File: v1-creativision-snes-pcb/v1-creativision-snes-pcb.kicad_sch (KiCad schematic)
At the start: 11 parts, among them J1 Left Joystick, J2 Right Joystick, J3 Power Entry, J4 PS/2 Keyboard, J5 SNES, SW1 Reset Pico, U1 Pico

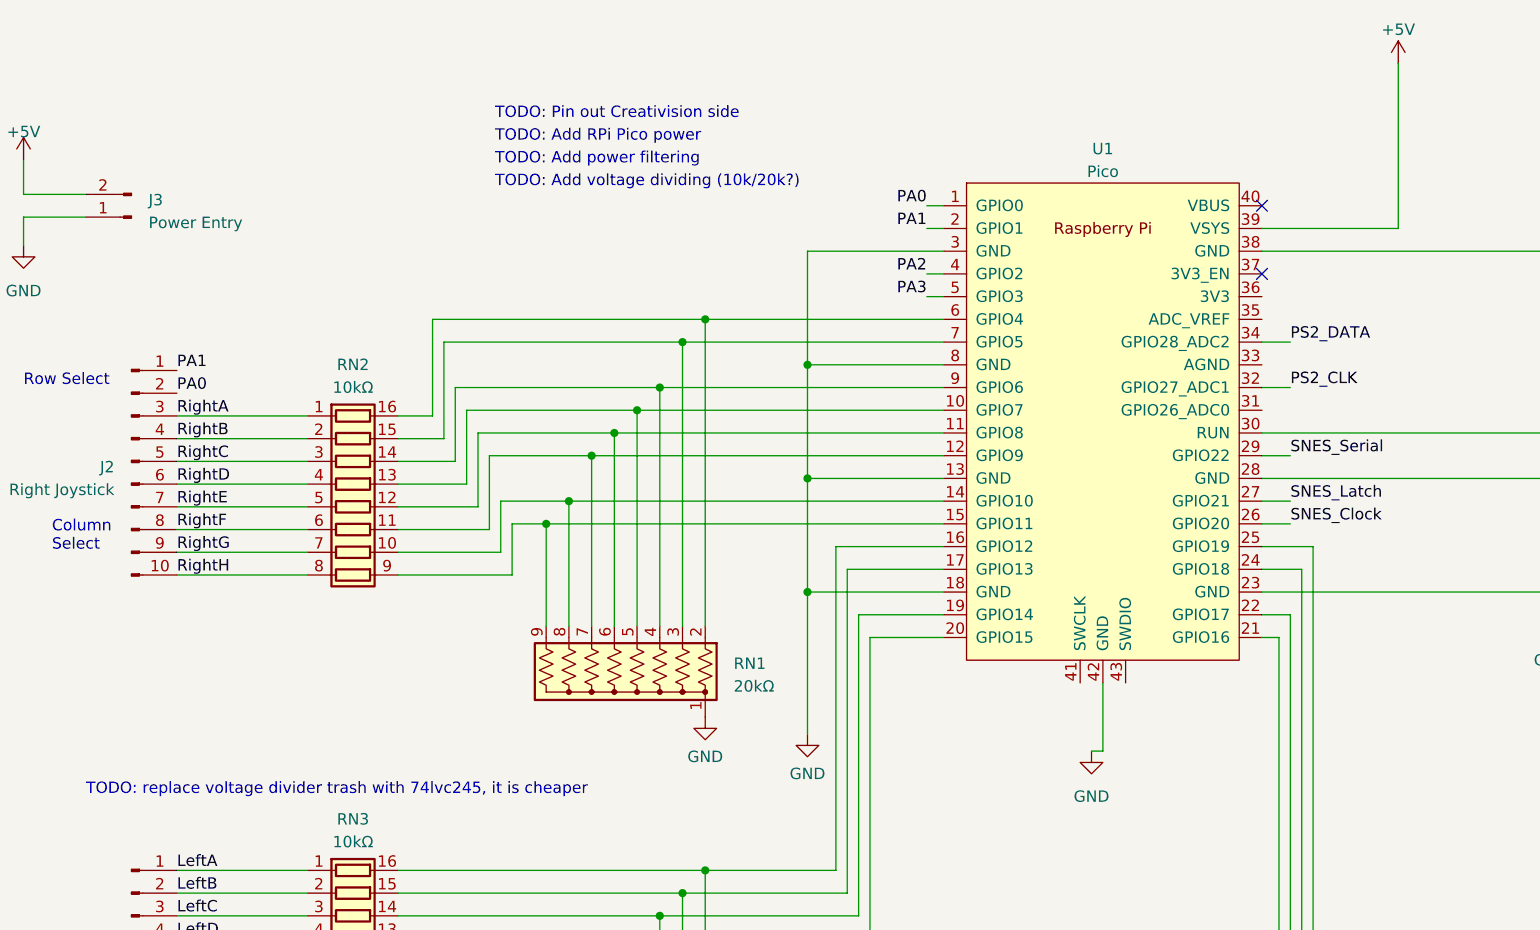
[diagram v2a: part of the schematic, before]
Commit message: Use 74lvc245 instead of voltage divider
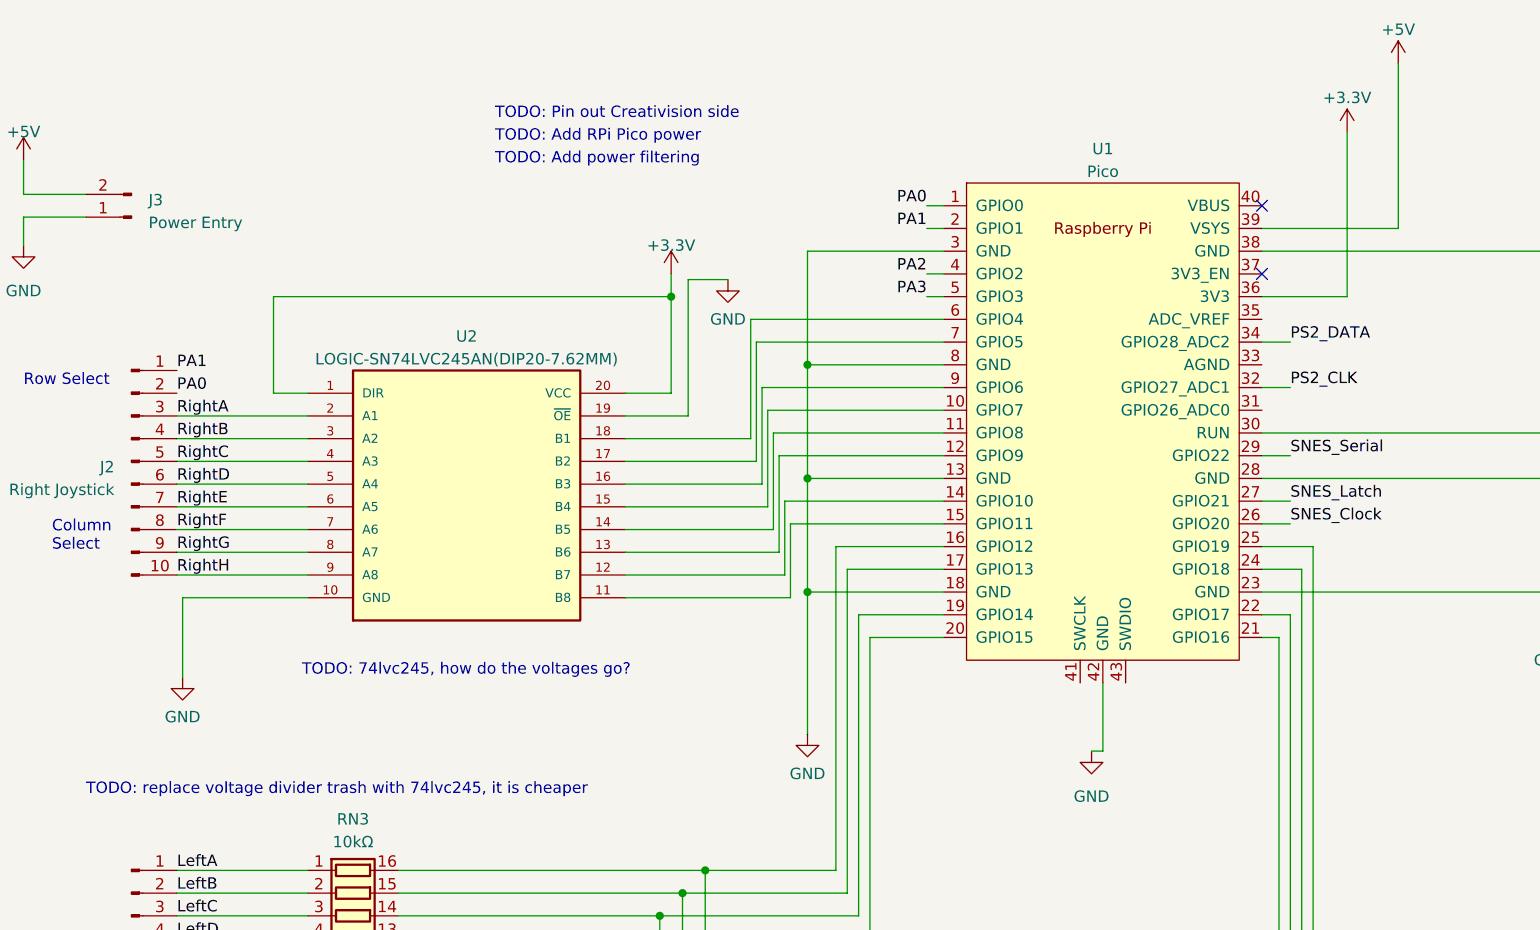
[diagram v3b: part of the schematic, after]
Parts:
- removed RN1: 20kΩ, Resistor_THT:R_Array_SIP9, symbol Device:R_Network08_US
- removed RN2: 10kΩ, symbol Device:R_Pack08
- added U2: LOGIC-SN74LVC245AN(DIP20-7.62MM), Package_DIP:DIP-20_W7.62mm_Socket_LongPads, symbol LOGIC-SN74LVC245AN_DIP20-7.62MM_:LOGIC-SN74LVC245AN(DIP20-7.62MM)
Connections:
- net GND: now also U2.10 (GND), U2.19 (~{OE})
- net RightA: now also U2.2 (A1)
- net RightB: now also U2.3 (A2)
- net RightC: now also U2.4 (A3)
- net RightD: now also U2.5 (A4)
- net RightE: now also U2.6 (A5)
- net RightF: now also U2.7 (A6)
- net RightG: now also U2.8 (A7)
- net RightH: now also U2.9 (A8)
- net at U1.6 (GPIO4): now also U2.18 (B1)
- net at U1.7 (GPIO5): now also U2.17 (B2)
- net at U1.9 (GPIO6): now also U2.16 (B3)
- net at U1.10 (GPIO7): now also U2.15 (B4)
- net at U1.11 (GPIO8): now also U2.14 (B5)
- net at U1.12 (GPIO9): now also U2.13 (B6)
- net at U1.14 (GPIO10): now also U2.12 (B7)
- net at U1.15 (GPIO11): now also U2.11 (B8)
- net +3.3V: now reaches U1.36 (3V3)
- net +3.3V: now also U2.1 (DIR), U2.20 (VCC)
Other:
- note added: "TODO: 74lvc245, how do the voltages go?"
- note removed: "TODO: Add voltage dividing (10k/20k?)"

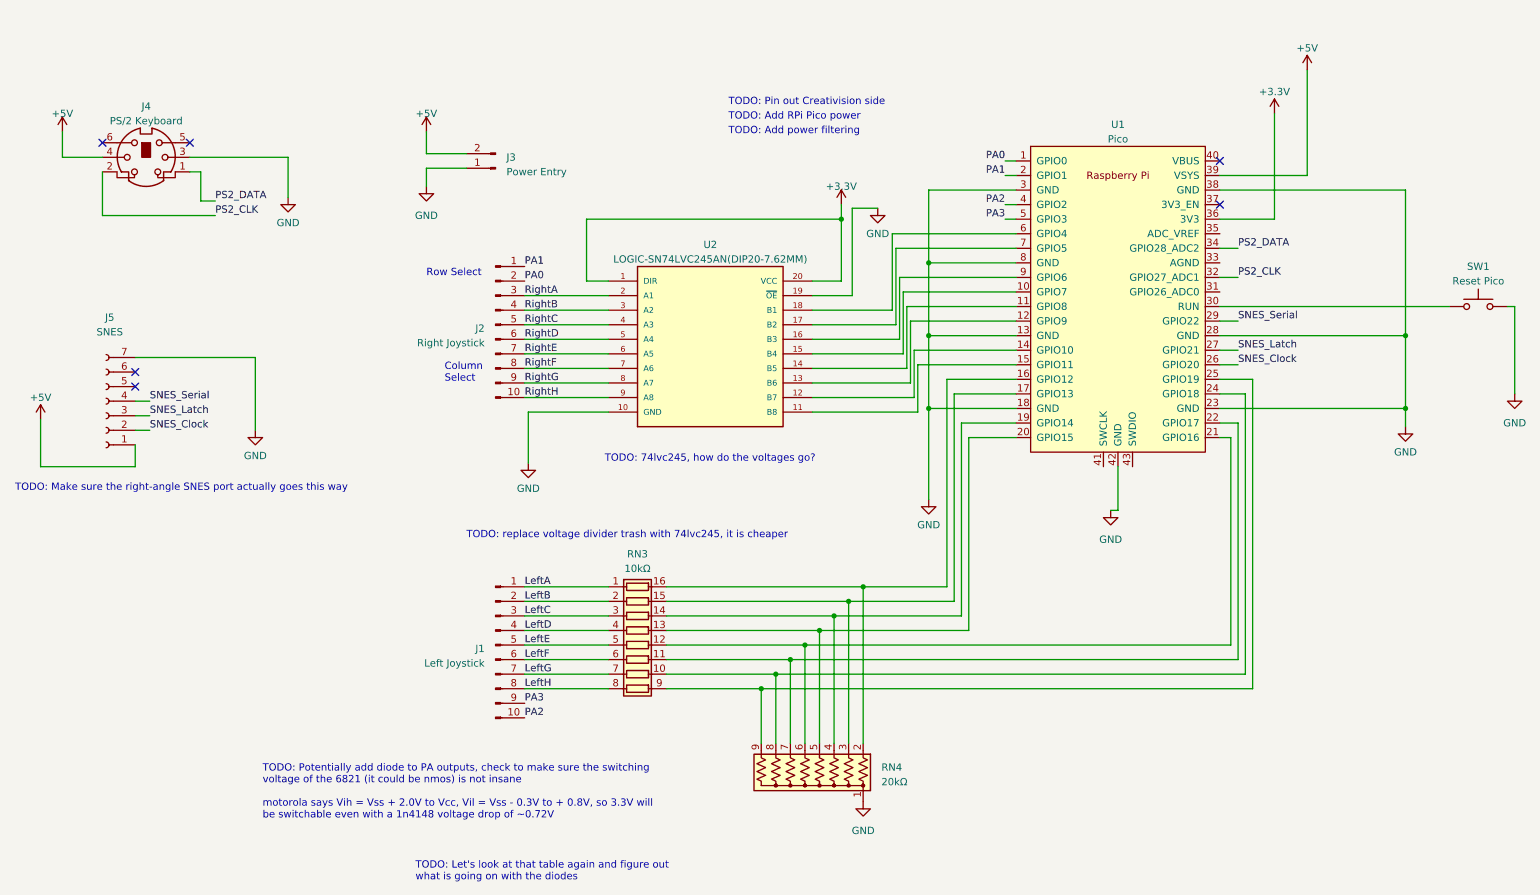
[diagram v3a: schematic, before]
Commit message: PCB all joined up with the lvc strategy
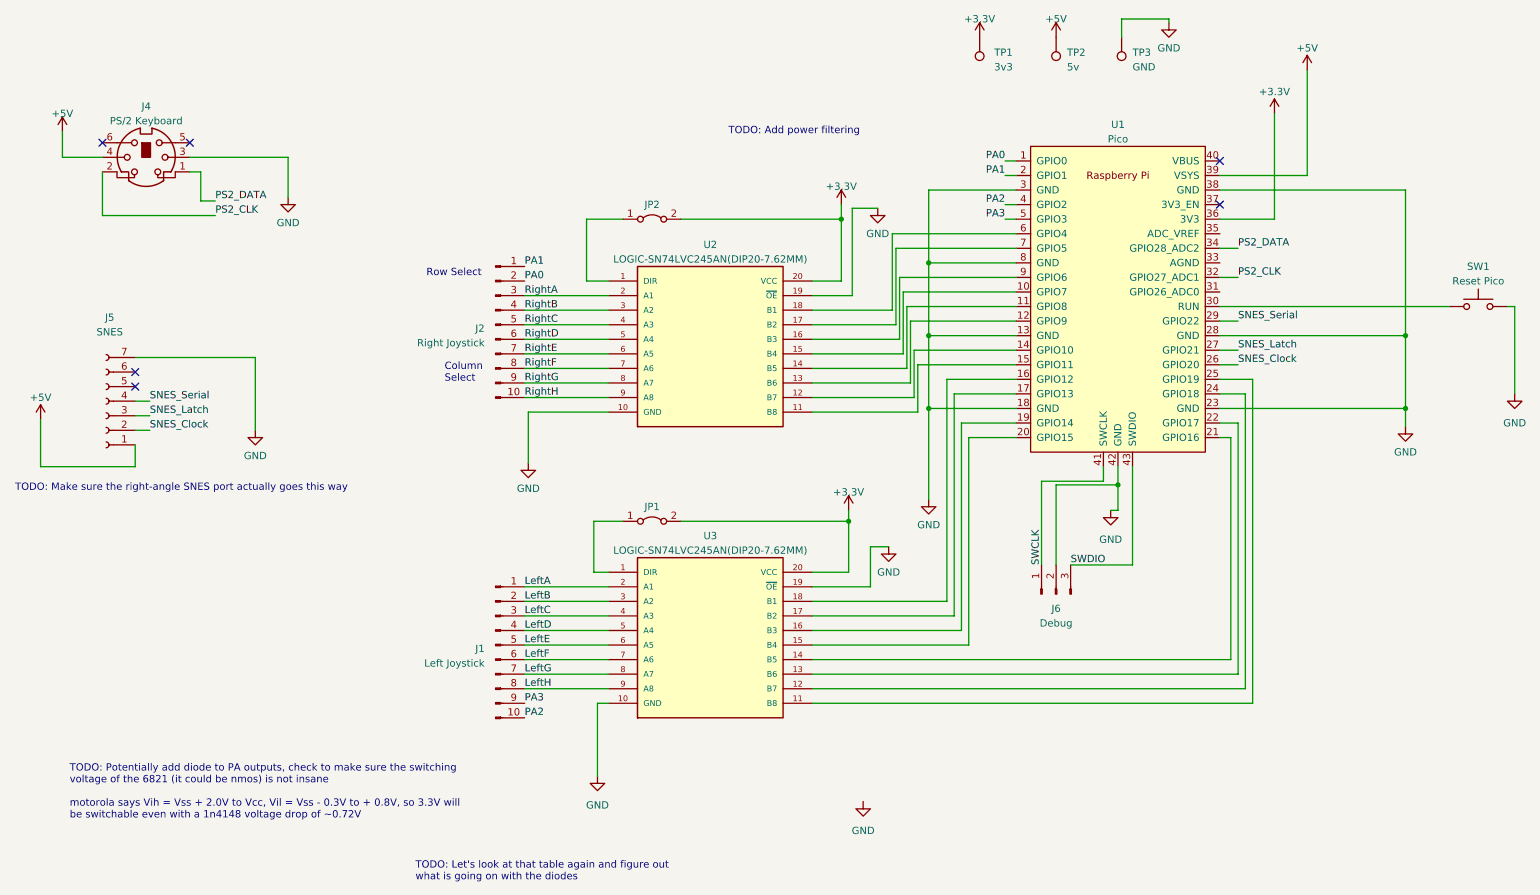
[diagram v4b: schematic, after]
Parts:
- removed J3: Power Entry, Connector_PinHeader_2.54mm:PinHeader_1x02_P2.54mm_Vertical, symbol Connector:Conn_01x02_Pin
- removed RN3: 10kΩ, symbol Device:R_Pack08
- removed RN4: 20kΩ, Resistor_THT:R_Array_SIP9, symbol Device:R_Network08_US
- added J6: Debug, Connector_PinHeader_2.54mm:PinHeader_1x03_P2.54mm_Vertical, symbol Connector:Conn_01x03_Pin
- added JP1, JP2: Jumper_2_Bridged, Jumper:SolderJumper-2_P1.3mm_Bridged2Bar_Pad1.0x1.5mm, symbol Jumper:Jumper_2_Bridged
- added TP1: 3v3, TestPoint:TestPoint_Loop_D1.80mm_Drill1.0mm_Beaded, symbol Connector:TestPoint
- added TP2: 5v, TestPoint:TestPoint_Loop_D1.80mm_Drill1.0mm_Beaded, symbol Connector:TestPoint
- added TP3: GND, TestPoint:TestPoint_Loop_D1.80mm_Drill1.0mm_Beaded, symbol Connector:TestPoint
- added U3: LOGIC-SN74LVC245AN(DIP20-7.62MM), Package_DIP:DIP-20_W7.62mm_Socket_LongPads, symbol LOGIC-SN74LVC245AN_DIP20-7.62MM_:LOGIC-SN74LVC245AN(DIP20-7.62MM)
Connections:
- net +3.3V: now also JP1.2 (B), JP2.2 (B), TP1.1, U3.20 (VCC); no longer U2.1 (DIR)
- net +5V: now also TP2.1
- net GND: now also J6.2 (Pin_2), TP3.1, U3.10 (GND), U3.19 (~{OE})
- net LeftA: now also U3.2 (A1)
- net LeftB: now also U3.3 (A2)
- net LeftC: now also U3.4 (A3)
- net LeftD: now also U3.5 (A4)
- net LeftE: now also U3.6 (A5)
- net LeftF: now also U3.7 (A6)
- net LeftG: now also U3.8 (A7)
- net LeftH: now also U3.9 (A8)
- net at U1.16 (GPIO12): now also U3.18 (B1)
- net at U1.17 (GPIO13): now also U3.17 (B2)
- net at U1.19 (GPIO14): now also U3.16 (B3)
- net at U1.20 (GPIO15): now also U3.15 (B4)
- net at U1.21 (GPIO16): now also U3.14 (B5)
- net at U1.22 (GPIO17): now also U3.13 (B6)
- net at U1.24 (GPIO18): now also U3.12 (B7)
- net at U1.25 (GPIO19): now also U3.11 (B8)
- net SWCLK: now reaches U1.41 (SWCLK)
- net SWCLK: now also J6.1 (Pin_1)
- net SWDIO: now reaches U1.43 (SWDIO)
- net SWDIO: now also J6.3 (Pin_3)
- new net: JP2.1 (A), U2.1 (DIR)
- new net: JP1.1 (A), U3.1 (DIR)
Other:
- note removed: "TODO: 74lvc245, how do the voltages go?"
- note removed: "TODO: Add RPi Pico power"
- note removed: "TODO: Pin out Creativision side"
- note removed: "TODO: replace voltage divider trash with 74lvc245, it is cheaper"

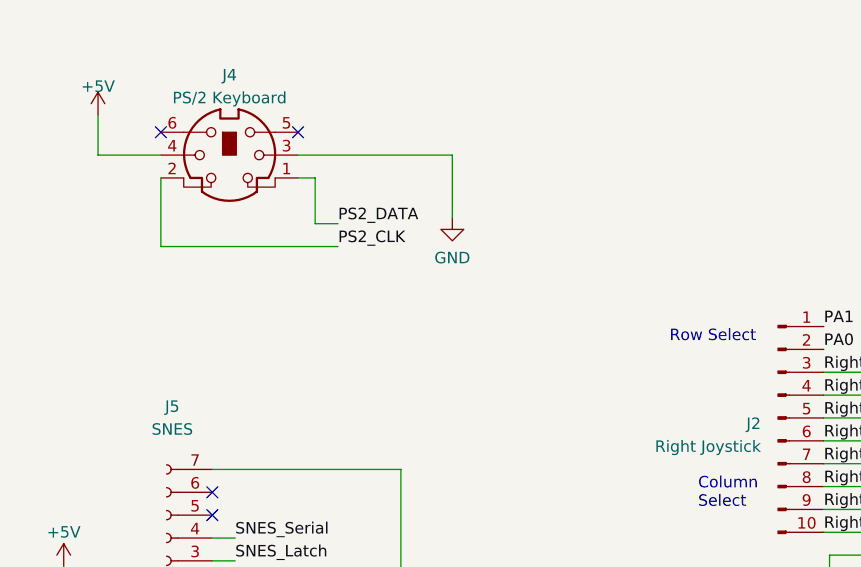
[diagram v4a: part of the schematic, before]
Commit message: Basics of SNES reading (untested)
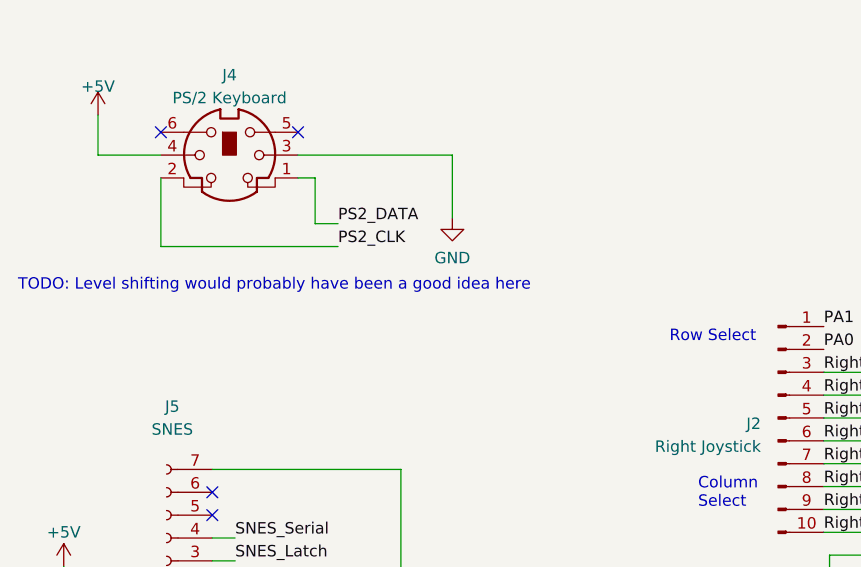
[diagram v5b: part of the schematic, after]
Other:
- note added: "TODO: Level shifting would probably have been a good idea here"
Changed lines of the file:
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@@
+    (effects (font (size 1.27 1.27)) (justify left bottom))
+  )
+  (text "TODO: Level shifting would probably have been a good idea here"
+    (at 12.7 64.77 0)
     (effects (font (size 1.27 1.27)) (justify left bottom))
   )
